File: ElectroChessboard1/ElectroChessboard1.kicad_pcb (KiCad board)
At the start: 2 copper layers, 306.2 x 314.8 mm, 241 parts, among them IC1 A3213ELHLT-T, IC10 A3213ELHLT-T, IC11 A3213ELHLT-T, IC12 A3213ELHLT-T, IC13 A3213ELHLT-T, IC14 A3213ELHLT-T, IC15 A3213ELHLT-T, IC16 A3213ELHLT-T, IC17 A3213ELHLT-T, IC18 ADG708BRUZ-REEL7, IC19 A3213ELHLT-T, IC2 A3213ELHLT-T, IC20 A3213ELHLT-T, IC21 A3213ELHLT-T, IC22 A3213ELHLT-T, IC23 A3213ELHLT-T, IC24 A3213ELHLT-T, IC25 A3213ELHLT-T, IC26 A3213ELHLT-T, IC27 A3213ELHLT-T, IC28 A3213ELHLT-T, IC29 A3213ELHLT-T, IC3 A3213ELHLT-T, IC30 A3213ELHLT-T, IC31 A3213ELHLT-T, IC32 A3213ELHLT-T, IC33 A3213ELHLT-T, IC34 A3213ELHLT-T, IC35 ADG708BRUZ-REEL7, IC36 ADG708BRUZ-REEL7, IC37 A3213ELHLT-T, IC38 A3213ELHLT-T, IC39 A3213ELHLT-T, IC4 A3213ELHLT-T, IC40 A3213ELHLT-T, IC41 A3213ELHLT-T, IC42 A3213ELHLT-T, IC43 A3213ELHLT-T, IC44 A3213ELHLT-T, IC45 A3213ELHLT-T, IC46 A3213ELHLT-T, IC47 A3213ELHLT-T, IC48 A3213ELHLT-T, IC49 A3213ELHLT-T, IC5 A3213ELHLT-T, IC50 A3213ELHLT-T, IC51 A3213ELHLT-T, IC52 A3213ELHLT-T, IC53 ADG708BRUZ-REEL7, IC54 ADG708BRUZ-REEL7, IC55 A3213ELHLT-T, IC56 A3213ELHLT-T, IC57 A3213ELHLT-T, IC58 A3213ELHLT-T, IC59 A3213ELHLT-T, IC6 A3213ELHLT-T, IC60 A3213ELHLT-T, IC61 A3213ELHLT-T, IC62 A3213ELHLT-T, IC63 A3213ELHLT-T, IC64 A3213ELHLT-T, IC65 A3213ELHLT-T, IC66 A3213ELHLT-T, IC67 A3213ELHLT-T, IC68 A3213ELHLT-T, IC69 A3213ELHLT-T, IC7 A3213ELHLT-T, IC70 A3213ELHLT-T, IC71 ADG708BRUZ-REEL7, IC72 ADG708BRUZ-REEL7, IC73 CD74HC154M96, IC74 CD74HC154M96, IC75 DS1307Z+T&R, IC76 CD74HC154M96, IC77 CD74HC154M96, IC8 A3213ELHLT-T, IC9 ADG708BRUZ-REEL7, J1 USB_B, J3 Conn_01x04_Pin, J5 Conn_01x06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

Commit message: Layout done
Now wiring is left, and few parts that do not need specific placement
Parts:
- moved R1 595.7 mm to (475.1, 283.8)
- moved R38 595.7 mm to (475.4, 279.6)
- moved R39 595.7 mm to (475.4, 281.8)
- moved C1 595.7 mm to (471.9, 279.7)
- moved C3 595.7 mm to (471.9, 282.0)
- moved C4 595.7 mm to (471.9, 284.3)
- moved D3 595.7 mm to (473.1, 287.1)
- moved IC75 595.7 mm to (465.9, 281.8)
- moved U2 593.6 mm to (441.8, 297.8)
- moved Y1 586.7 mm to (463.2, 295.4)
- moved Y3 586.7 mm to (469.4, 301.0)
- moved J6 578.4 mm to (447.6, 326.0)
- moved U3 551.2 mm to (470.6, 336.4)
- moved C10 550.9 mm to (478.2, 317.5)
- moved C5 550.9 mm to (478.2, 312.9)
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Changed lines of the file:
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@@
 	(footprint "SamacSys_Parts:CAPC1608X90N"
 		(layer "F.Cu")
-		(at -43.305 140.04)
+		(at 478.225 317.5)
 		(descr "CL10C220JB8NNNC")
 		(tags "Capacitor")
@@
 	(footprint "SamacSys_Parts:1027"
 		(layer "F.Cu")
-		(at -117.5 98.75)
+		(at 441.75 297.75)
 		(descr "1027-3")
 		(tags "Undefined or Miscellaneous")
@@
 	(footprint "SamacSys_Parts:SOIC127P600X175-8N"
 		(layer "F.Cu")
-		(at -93.635 77.29)
+		(at 465.9 281.825)
 		(descr "soic8-ren3")
 		(tags "Integrated Circuit")
@@
 	(footprint "SamacSys_Parts:CAPC1608X90N"
 		(layer "F.Cu")
-		(at -87.635 79.74)
+		(at 471.9 284.275)
 		(descr "CL10C220JB8NNNC")
 		(tags "Capacitor")
@@
 	(footprint "SamacSys_Parts:SOIC127P1030X265-24N"
 		(layer "F.Cu")
-		(at 109.525 285.575)
+		(at 113.25 284.715)
 		(descr "DW (R-PDSO-G24)")
 		(tags "Integrated Circuit")
@@
 	(footprint "SamacSys_Parts:CAPC1608X90N"
 		(layer "F.Cu")
-		(at -43.305 135.46)
+		(at 478.225 312.92)
 		(descr "CL10C220JB8NNNC")
 		(tags "Capacitor")
@@
 	(footprint "SamacSys_Parts:RESC1005X40N"
 		(layer "F.Cu")
-		(at -84.185 77.24)
+		(at 475.35 281.775)
 		(descr "0402")
 		(tags "Resistor")
@@
 	(footprint "SamacSys_Parts:RESC1005X40N"
 		(layer "F.Cu")
-		(at -84.185 75.09)
+		(at 475.35 279.625)
 		(descr "0402")
 		(tags "Resistor")
@@
 	(footprint "SamacSys_Parts:SOIC127P1030X265-24N"
 		(layer "F.Cu")
-		(at 179.55 284.35)
+		(at 179.75 284.75)
 		(descr "DW (R-PDSO-G24)")
 		(tags "Integrated Circuit")
@@
 	(footprint "SamacSys_Parts:0603L050SLYR"
 		(layer "F.Cu")
-		(at -38.605 136.365)
+		(at 482.925 313.825)
 		(descr "0603L050SLYR")
 		(tags "Resettable Fuse")
@@
 	(footprint "Connector_PinSocket_2.00mm:PinSocket_1x06_P2.00mm_Vertical_SMD_Pin1Right"
 		(layer "F.Cu")
-		(at -91.3 115.99)
+		(at 447.65 326)
 		(descr "surface-mounted straight socket strip, 1x06, 2.00mm pitch, single row, style 2 (pin 1 right) (https://www.jayconsystems.com/fileuploader/download/download/?d=1&file=custom%2Fupload%2FFile-1375728122.pdf), script generated")
 		(tags "Surface mounted socket strip SMD 1x06 2.00mm single row style2 pin1 right")
@@
 	(footprint "SamacSys_Parts:SOIC127P1030X265-24N"
 		(layer "F.Cu")
-		(at 132.025 287.305)
+		(at 145.275 284.695)
 		(descr "DW (R-PDSO-G24)")
 		(tags "Integrated Circuit")
@@
 	(footprint "Package_SO:SSOP-28_5.3x10.2mm_P0.65mm"
 		(layer "F.Cu")
-		(at -39.78 128.29)
+		(at 470.65 336.425)
 		(descr "28-Lead Plastic Shrink Small Outline (SS)-5.30 mm Body [SSOP] (see Microchip Packaging Specification 00000049BS.pdf)")
 		(tags "SSOP 0.65")
@@
 	(footprint "SamacSys_Parts:BEADC1608X95N"
 		(layer "F.Cu")
-		(at -39.53 139.69)
+		(at 482 317.15)
 		(descr "GZ1608D601TF*-*")
 		(tags "Ferrite Bead")
@@
 	(footprint "Package_QFP:TQFP-100_14x14mm_P0.5mm"
 		(layer "F.Cu")
-		(at -91.05 96.29)
+		(at 295.5 303)
 		(descr "TQFP, 100 Pin (http://www.microsemi.com/index.php?option=com_docman&task=doc_download&gid=131095), generated with kicad-footprint-generator ipc_gullwing_generator.py")
 		(tags "TQFP QFP")
@@
 	(footprint "Capacitor_SMD:CP_Elec_4x5.4"
 		(layer "F.Cu")
-		(at -59.97 143.24)
+		(at 461.56 320.7)
 		(descr "SMD capacitor, aluminum electrolytic, Panasonic A5 / Nichicon, 4.0x5.4mm")
 		(tags "capacitor electrolytic")
@@
 	(footprint "SamacSys_Parts:CAPC1608X90N"
 		(layer "F.Cu")
-		(at -43.305 137.75)
+		(at 478.225 315.21)
 		(descr "CL10C220JB8NNNC")
 		(tags "Capacitor")
@@
 	(footprint "Connector_USB:USB_B_Lumberg_2411_02_Horizontal"
 		(layer "F.Cu")
-		(at -61.235 130.04)
+		(at 309.7125 253.75)
 		(descr "USB 2.0 receptacle type B, horizontal version, through-hole, https://downloads.lumberg.com/datenblaetter/en/2411_02.pdf")
 		(tags "USB B receptacle horizontal through-hole")
@@
 		)
 		(fp_text user "${REFERENCE}"
-			(at 7.5 1.25 180)
+			(at 7.5 1.25 0)
 			(layer "F.Fab")
 			(effects
@@
 		)
 		(embedded_fonts no)
-		(model "${KICAD9_3DMODEL_DIR}/Connector_USB.3dshapes/USB_B_Lumberg_2411_02_Horizontal.wrl"
+		(model "${KICAD9_3DMODEL_DIR}/Connector_USB.3dshapes/USB-B1HSB6--3DModel-STEP-1.STEP"
 			(offset
-				(xyz 0 0 0)
+				(xyz 7 -1.25 0)
 			)
 			(scale
@@
 			)
 			(rotate
-				(xyz 0 0 0)
+				(xyz -90 -0 -90)
 			)
 		)
@@
 	(footprint "Resistor_SMD:R_0402_1005Metric"
 		(layer "F.Cu")
-		(at -84.43 79.31)
+		(at 475.105 283.845)
 		(descr "Resistor SMD 0402 (1005 Metric), square (rectangular) end terminal, IPC_7351 nominal, (Body size source: IPC-SM-782 page 72, https://www.pcb-3d.com/wordpress/wp-content/uploads/ipc-sm-782a_amendment_1_and_2.pdf), generated with kicad-footprint-generator")
 		(tags "resistor")
@@
 	(footprint "Crystal:Crystal_SMD_HC49-SD"
 		(layer "F.Cu")
-		(at -92.9 108.59)
+		(at 463.25 295.415)
 		(descr "SMD Crystal HC-49-SD http://cdn-reichelt.de/documents/datenblatt/B400/xxx-HC49-SMD.pdf, 11.4x4.7mm^2 package")
 		(tags "SMD SMT crystal")
@@
 	(footprint "SamacSys_Parts:CAPC1608X90N"
 		(layer "F.Cu")
-		(at -87.635 75.16)
+		(at 471.9 279.695)
 		(descr "CL10C220JB8NNNC")
 		(tags "Capacitor")
@@
 	(footprint "SamacSys_Parts:RESC1005X40N"
 		(layer "F.Cu")
-		(at 106.74 296.5)
+		(at 110.45 296)
 		(descr "0402")
 		(tags "Resistor")
@@
 	(footprint "SamacSys_Parts:SODFL1608X70N"
 		(layer "F.Cu")
-		(at -39.81 142.04)
+		(at 481.72 319.5)
 		(descr "sod-523")
 		(tags "Diode")
@@
 	(footprint "Diode_SMD:D_SOD-123"
 		(layer "F.Cu")
-		(at -86.465 82.56)
+		(at 473.07 287.095)
 		(descr "SOD-123")
 		(tags "SOD-123")
@@
 	(footprint "SamacSys_Parts:CAPC1608X90N"
 		(layer "F.Cu")
-		(at 111.79 296.75)
+		(at 115.5 296.25)
 		(descr "CL10C220JB8NNNC")
 		(tags "Capacitor")
@@
 	(footprint "SamacSys_Parts:CAPC1608X90N"
 		(layer "F.Cu")
-		(at 129.79 298.25)
+		(at 143 295.5)
 		(descr "CL10C220JB8NNNC")
 		(tags "Capacitor")
@@
 	(footprint "SamacSys_Parts:CAPC1608X90N"
 		(layer "F.Cu")
-		(at -87.635 77.45)
+		(at 471.9 281.985)
 		(descr "CL10C220JB8NNNC")
 		(tags "Capacitor")
@@
 	(footprint "Crystal:Crystal_C38-LF_D3.0mm_L8.0mm_Vertical"
 		(layer "F.Cu")
-		(at -86.8 114.19)
+		(at 469.35 301.015)
 		(descr "Crystal THT C38-LF 8.0mm length 3.0mm diameter")
 		(tags "['C38-LF']")
@@
 	(footprint "Connector_PinSocket_2.54mm:PinSocket_1x06_P2.54mm_Horizontal"
 		(layer "F.Cu")
-		(at 110 305.84)
+		(at 107.65 305.425)
 		(descr "Through hole angled socket strip, 1x06, 2.54mm pitch, 8.51mm socket length, single row (from Kicad 4.0.7), script generated")
 		(tags "Through hole angled socket strip THT 1x06 2.54mm single row")
@@
 	(footprint "Diode_SMD:D_SMA"
 		(layer "F.Cu")
-		(at -52.025 142.59)
+		(at 469.505 320.05)
 		(descr "Diode SMA (DO-214AC)")
 		(tags "Diode SMA (DO-214AC)")
@@
 	(footprint "SamacSys_Parts:RESC1005X40N"
 		(layer "F.Cu")
-		(at 133.95 298.25)
+		(at 147.16 295.5)
 		(descr "0402")
 		(tags "Resistor")
@@
 	(footprint "SamacSys_Parts:SOIC127P1030X265-24N"
 		(layer "F.Cu")
-		(at 239.8 284.445)
+		(at 239.8 284.75)
 		(descr "DW (R-PDSO-G24)")
 		(tags "Integrated Circuit")
@@
 	)
 	(gr_rect
-		(start 19.85 289.665)
-		(end 99.85 334.665)
+		(start 19.85 289.25)
+		(end 99.85 334.25)
 		(stroke
 			(width 0.1)
@@
 	)
 	(gr_text "SD card\nreader"
-		(at 63.85 312.165 90)
+		(at 63.85 311.75 90)
 		(layer "F.SilkS")
 		(effects

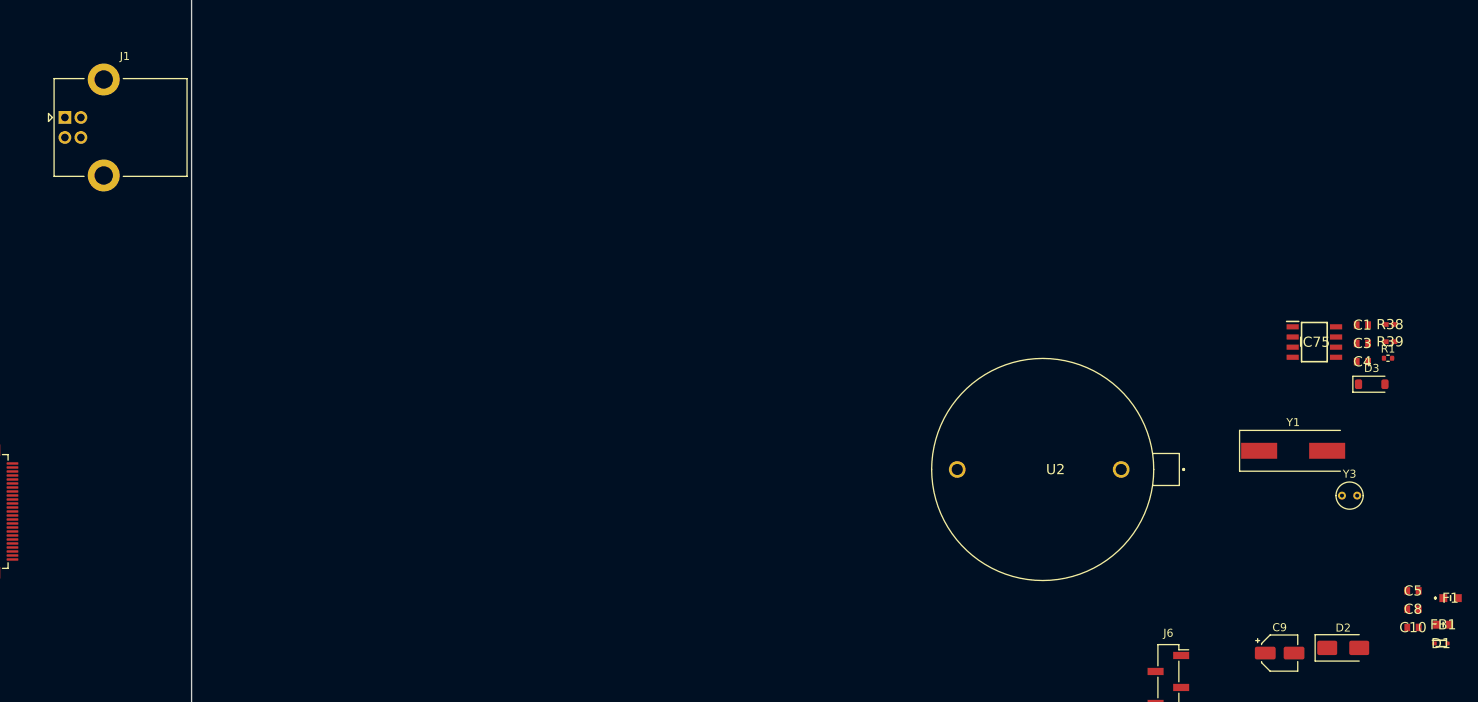
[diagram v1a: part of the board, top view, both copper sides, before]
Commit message: Updated PCB
usb-c
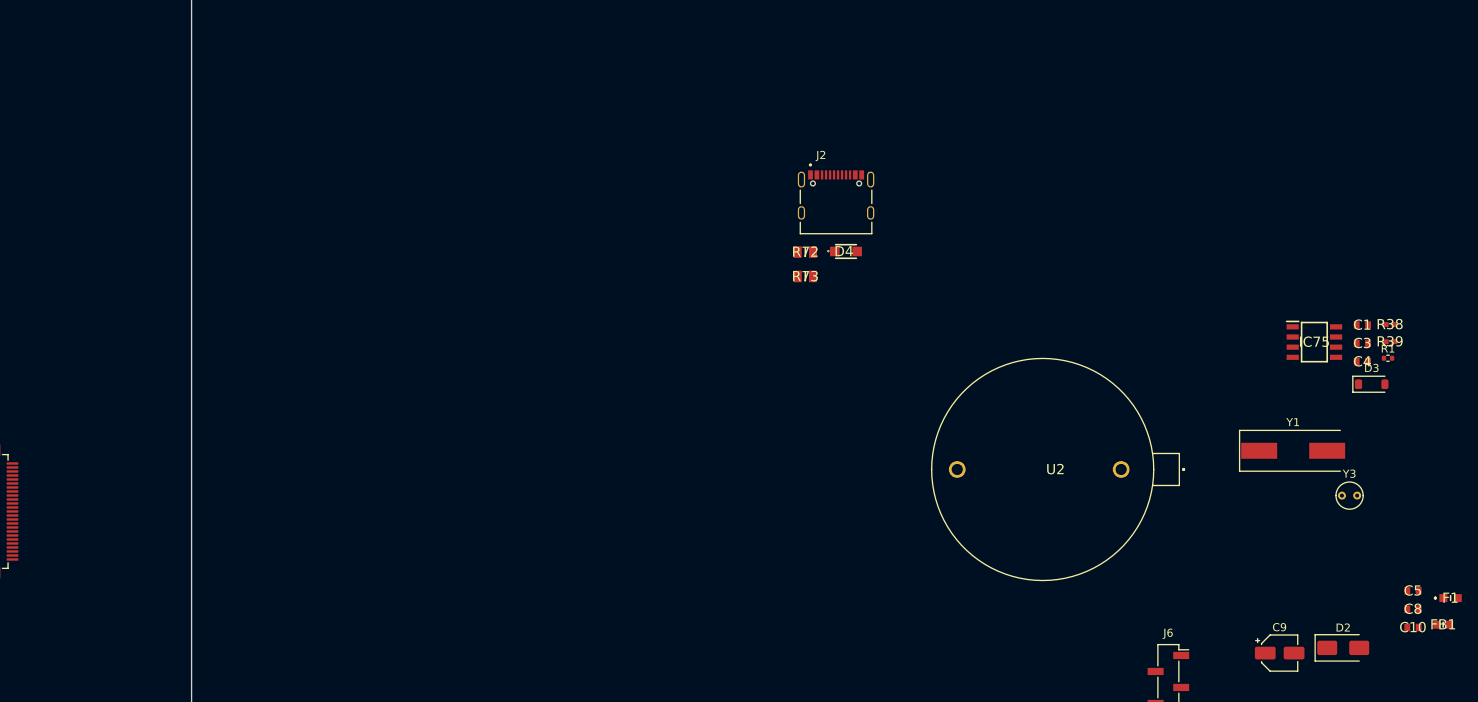
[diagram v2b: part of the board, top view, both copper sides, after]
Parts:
- removed D1: ESD5Z5V0, SamacSys_Parts:SODFL1608X70N
- removed J1: USB_B, Connector_USB:USB_B_Lumberg_2411_02_Horizontal
- added D4: PTVS5V0S1UTR,115, SamacSys_Parts:SOD123W, F.Cu at (407.4, 270.5)
- added J2: TYPE-C-31-M-12, TYPE-C-31-M-12:HRO_TYPE-C-31-M-12, F.Cu at (406.1, 265.7)
- added R72: 0805W8F5101T5E, SamacSys_Parts:RESC2013X65N, F.Cu at (402.3, 270.6)
- added R73: 0805W8F5101T5E, SamacSys_Parts:RESC2013X65N, F.Cu at (402.3, 273.6)
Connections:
- net Net-(D1-K) renamed VBUS

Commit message: Chessboard GNDs wired
Chessboard GNDs wired
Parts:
- moved U2 225.2 mm to (217.0, 311.2)
- moved J2 85.7 mm to (322.5, 246.7), turned to 90 degrees
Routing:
- net SafeGND: track 0.00 -> 2392.7 mm
